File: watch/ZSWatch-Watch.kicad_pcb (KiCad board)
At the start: 4 copper layers, 37.2 x 38 mm, 62 parts, among them IC401 nPM1300-QEXX, IC501 APDS-9306-065, IC502 BMI270, IC503 LIS2MDLTR, IC504 BMP581, IC505 DRV2603RUNT, IC506 PCA9306JK, IC507 RV-8263-C8, IC601 FAN5622SX, IC602 USBLC6-2P6, IC603 MX25U51245GZ4I00, IC604 NTS0104GU12, M601 NORA-B106, X402 Battery, X509 Motor, X603 Device, X608 Display

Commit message: Add speaker
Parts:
- removed R503: 100k, Resistor_SMD:R_0201_0603Metric
- added LS801: Speaker, Same Sky:CMR-12062S-67, F.Cu at (191.8, 143.8)
- C502, MK501: moved to F.Cu
- moved C501 28.8 mm to (220.8, 128.5), turned to 45 degrees
- moved IC501 28.2 mm to (219.7, 127.2), turned to 45 degrees
- moved MK501 25.6 mm to (196.9, 139.6)
- moved C502 23.9 mm to (198.8, 140.8), turned to 90 degrees
- moved C509 20.7 mm to (214.1, 126.4), turned to 0 degrees
- moved C508 19.8 mm to (212.9, 127.2), turned to -90 degrees
- moved IC504 19.8 mm to (214.3, 127.7), turned to 90 degrees
- moved C504 15.9 mm to (210.5, 136.1), turned to -90 degrees
- moved IC502 15.6 mm to (212.2, 135.2), turned to -90 degrees
- moved C503 14.1 mm to (210.5, 134.2), turned to 90 degrees
- moved C506 11.1 mm to (211.1, 132.2), turned to 90 degrees
- moved C505 8.25 mm to (212.6, 130.7), turned to 180 degrees
- moved IC503 8.24 mm to (212.6, 132.2), turned to 180 degrees
- moved IC505 7.66 mm to (199.4, 142.9), turned to 180 degrees
- moved C507 5.86 mm to (214.0, 132.3), turned to -90 degrees
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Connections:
- M601 pad C8: /Project Architecture/MCU/~{RTC-INT} -> /Project Architecture/Extension/PA-BCLK
- M601 pad D3: /Project Architecture/Extension/Status -> /Project Architecture/Extension/~{RESET_{HR}}
- M601 pad E3: /Project Architecture/Extension/~{RESET_{HR}} -> /Project Architecture/Extension/Status
- M601 pad E7: /Project Architecture/Extension/PA-BCLK -> /Project Architecture/MCU/BMI270-INT
- M601 pad F7: unconnected-(M601C-P1.07-PadF7) -> /Project Architecture/MCU/LIS2MDL-INT
- M601 pad F8: /Project Architecture/MCU/MIC-CLK -> unconnected-(M601C-P1.14-PadF8)
- M601 pad F9: /Project Architecture/MCU/MIC-DATA -> /Project Architecture/MCU/~{RTC-INT}
- M601 pad G1: /Project Architecture/MCU/BMI270-INT -> /Project Architecture/MCU/VIB-EN
- M601 pad G2: /Project Architecture/MCU/VIB-EN -> /Project Architecture/MCU/MIC-DATA
- M601 pad G3: unconnected-(M601B-P0.25/AIN4-PadG3) -> /Project Architecture/MCU/MIC-CLK
- M601 pad H7: /Project Architecture/MCU/LIS2MDL-INT -> unconnected-(M601B-P0.29-PadH7)
- M801 pad S11: GND -> Net-(M801-SP_{N})
- M801 pad S112: /Project Architecture/Extension/~{RESET_{HR}} -> /Project Architecture/Extension/Status
- M801 pad S113: (no net) -> GND
- M801 pad S114: /Project Architecture/Extension/Status -> /Project Architecture/Extension/~{RESET_{HR}}
- M801 pad S12: /Project Architecture/Power Management/VSYS -> /Project Architecture/Extension/VHR
- M801 pad S13: (no net) -> Net-(M801-SP_{P})
- M801 pad S14: /Project Architecture/Extension/VHR -> /Project Architecture/Power Management/VSYS
- M801 pad S21: /Project Architecture/Extension/SP_{N} -> (no net)
- M801 pad S23: /Project Architecture/Extension/SP_{P} -> (no net)
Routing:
- net Net-(M801-SP_{P}): track 0.00 -> 19.5 mm, vias 0 -> 1
- net /Project Architecture/MCU/LIS2MDL-INT: track 37.5 -> 20.3 mm, vias 2 -> 3
- net Net-(M801-SP_{N}): track 0.00 -> 14.9 mm, vias 0 -> 1
- net /Project Architecture/Extension/SDA: track 71.2 -> 59.7 mm, vias 5 -> 3
- net /Project Architecture/MCU/BMI270-INT: track 23.4 -> 12.5 mm
- net /Project Architecture/MCU/MIC-CLK: track 13.5 -> 22.7 mm, vias 1 -> 2
- net /Project Architecture/Extension/VHR: track 46.3 -> 38.7 mm
- net /Project Architecture/Extension/SCL: track 70.4 -> 62.8 mm
- net /Project Architecture/MCU/VIB-EN: track 16.5 -> 10.6 mm
- net /Project Architecture/Extension/Status: track 16.8 -> 21.3 mm
- net /Project Architecture/Extension/PA-BCLK: track 14.5 -> 10.4 mm
- net /Project Architecture/Extension/~{RESET_{HR}}: track 21.1 -> 17.2 mm
- net /Project Architecture/MCU/VIB-PWM: track 16.4 -> 13.0 mm
- net /Project Architecture/Power Management/VSYS: track 60.0 -> 56.6 mm
- net USB-D-: track 20.1 -> 18.1 mm
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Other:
- board size 37.2 x 38 mm -> 37.4 x 37.5 mm

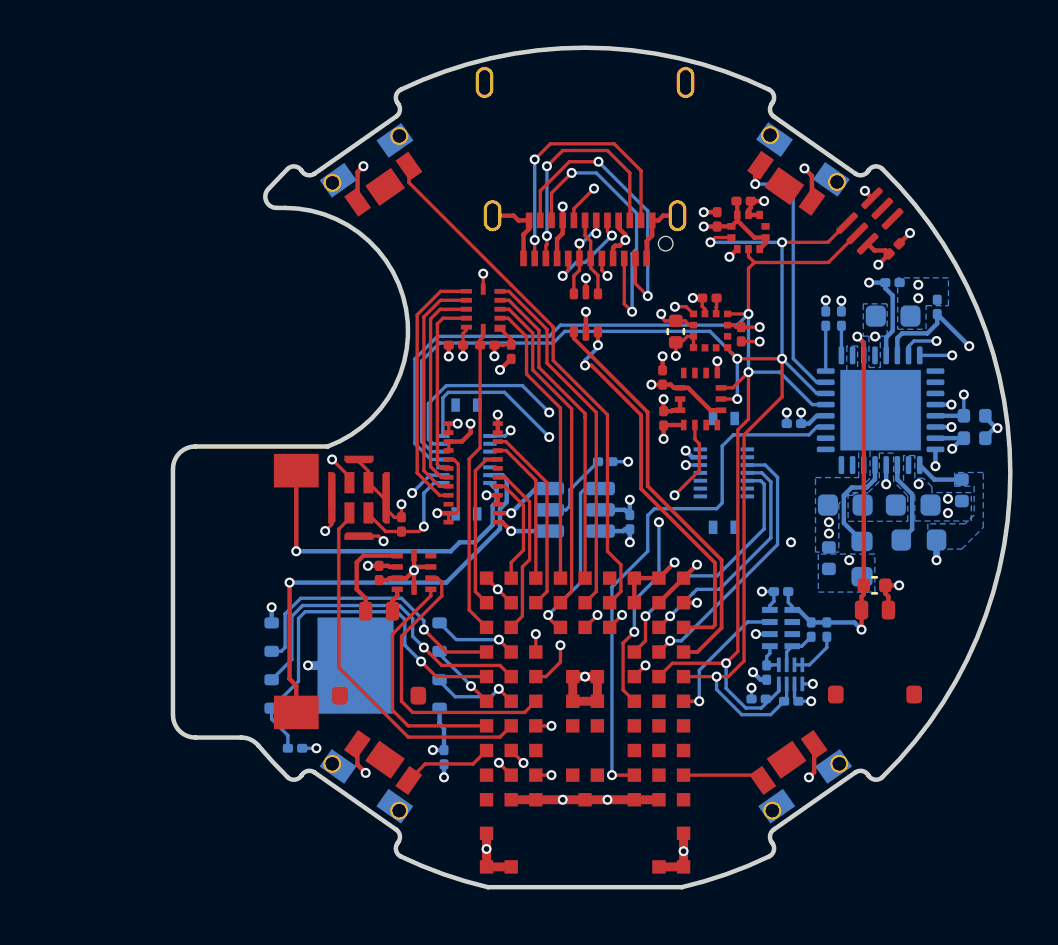
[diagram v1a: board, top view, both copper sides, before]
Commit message: New PCB outline, fix logo copy job for KiBot
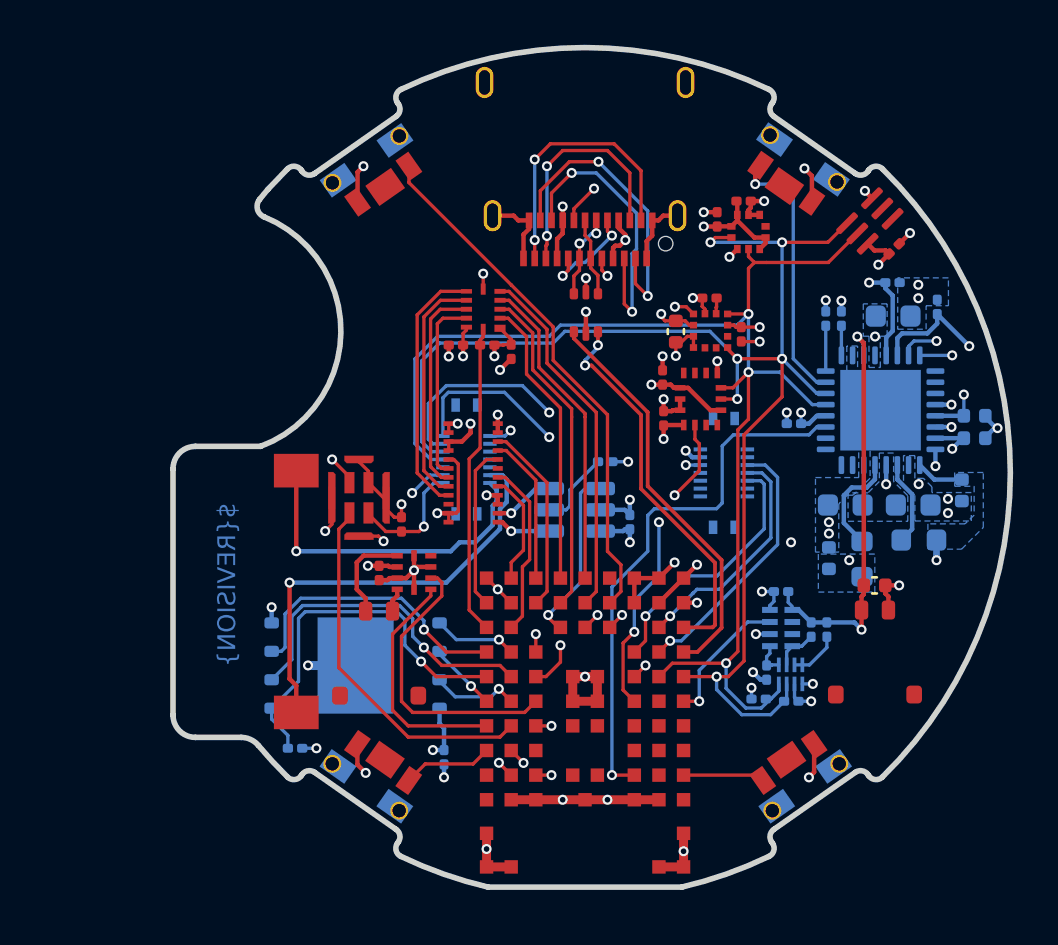
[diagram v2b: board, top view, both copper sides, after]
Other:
- outline, holes or cut-outs redrawn
- board text added: "${REVISION}"

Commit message: Move display connector 3 mm to the outside and optimize routing
Signed-off-by: Daniel Kampert <DanielKampert@kampis-elektroecke.de>
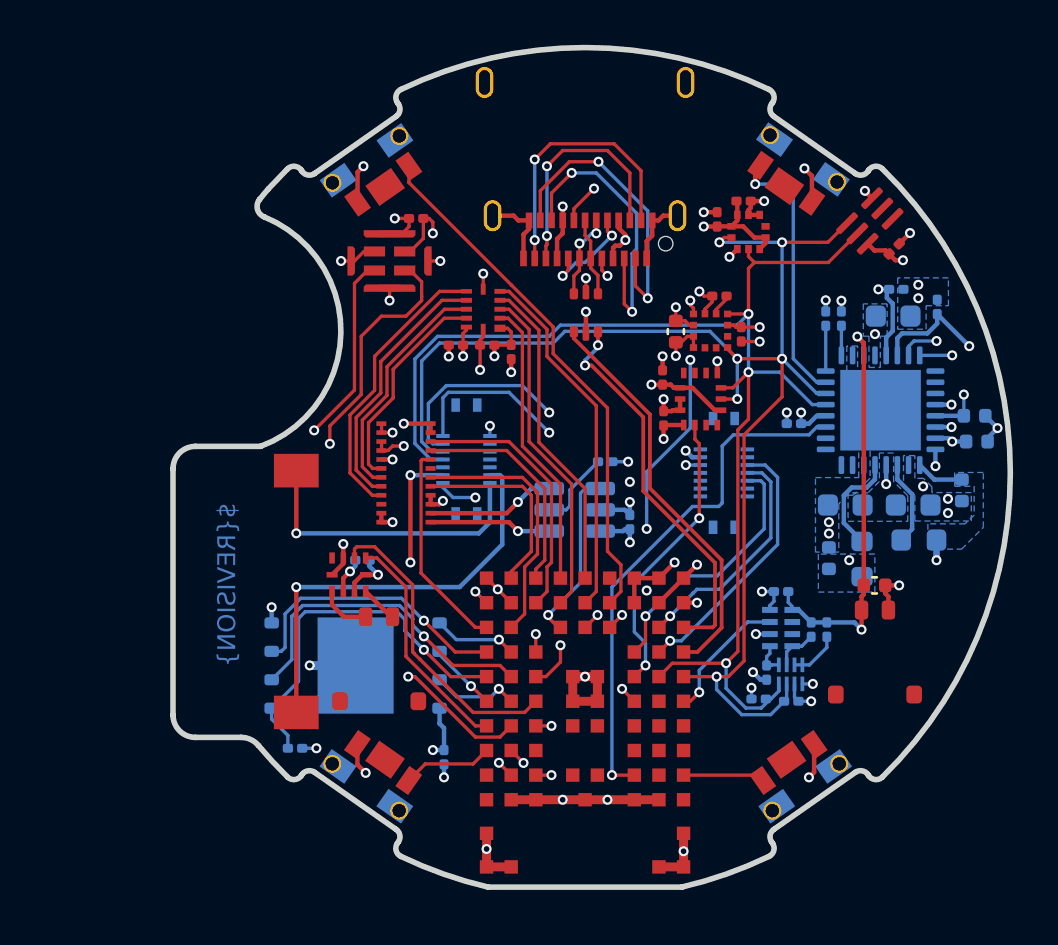
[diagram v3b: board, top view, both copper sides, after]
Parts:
- C510: moved to B.Cu
- moved C502 13.7 mm to (199.5, 127.1), turned to 180 degrees
- moved MK501 10.7 mm to (198.3, 129.0), turned to 90 degrees
- moved X608 3.00 mm to (199.0, 138.5)
- moved IC505 2.91 mm to (196.4, 143.1), turned to -90 degrees
- moved C510 0.94 mm to (197.1, 142.4), turned to 0 degrees
- moved C505 0.45 mm to (213.0, 130.6)
- moved C401 0.34 mm to (220.9, 130.3)
- moved X509 0.25 mm to (197.8, 146.8)
- moved C512 0.18 mm to (224.5, 137.1)
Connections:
- M601 pad B1: DISPLAY-CLK -> DISPLAY-EN
- M601 pad C1: DISPLAY-EN -> DISPLAY-CLK
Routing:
- net /Project Architecture/MCU/MIC-DATA: track 16.3 -> 28.4 mm, vias 0 -> 2
- net /Project Architecture/Extension/VHR: track 38.7 -> 47.7 mm, vias 2 -> 4
- net /Project Architecture/MCU/MIC-CLK: track 22.7 -> 30.7 mm
- net DISPLAY-DC: track 4.98 -> 8.74 mm
- net DISPLAY-DATA: track 7.83 -> 11.6 mm
- net DISPLAY-CS: track 6.62 -> 9.97 mm
- net DISPLAY-RST: track 8.53 -> 11.8 mm
- net GND: track 75.3 -> 72.1 mm, vias 54 -> 56
- net LEDK2: track 2.76 -> 5.76 mm
- net LEDK1: track 2.47 -> 5.47 mm
- net DISPLAY-CLK: track 7.32 -> 9.40 mm
- net Net-(IC505-OUT-): track 4.28 -> 2.32 mm
- net +3V0: track 42.3 -> 44.1 mm
- net Net-(M801-SP_{N}): track 14.9 -> 13.4 mm
- net /Project Architecture/Power Management/VSYS: track 56.6 -> 58.1 mm, vias 6 -> 7
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
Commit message: Fix wrong Extension footprint
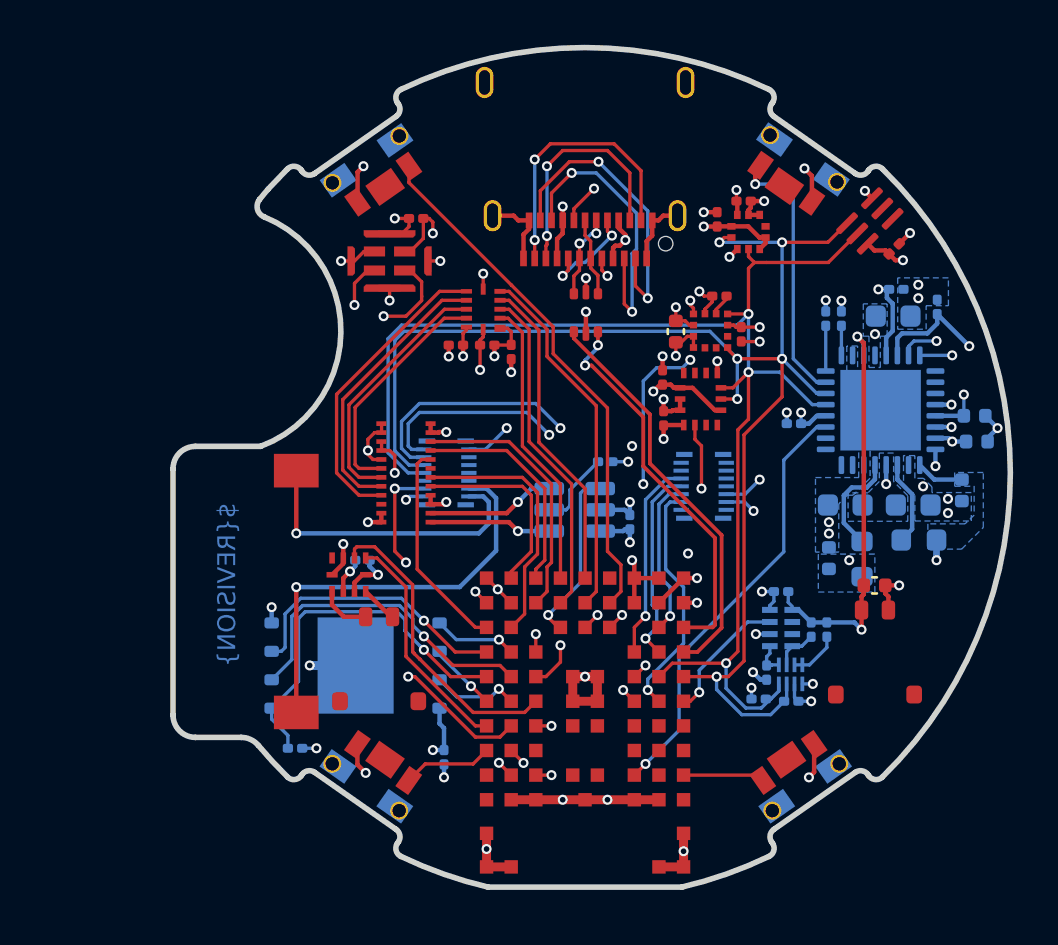
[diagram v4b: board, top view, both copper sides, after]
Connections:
- M601 pad C8: /Project Architecture/Extension/PA-BCLK -> /Project Architecture/Extension/PA-DIN
- M601 pad D8: /Project Architecture/Extension/PA-DIN -> /Project Architecture/Extension/PA-BCLK
- M601 pad F8: unconnected-(M601C-P1.14-PadF8) -> /Project Architecture/Extension/PA-MCLK
- M801 pad S211: (no net) -> /Project Architecture/Extension/PA-MCLK
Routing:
- net /Project Architecture/Extension/PA-MCLK: track 0.00 -> 10.7 mm, vias 0 -> 1
- net /Project Architecture/Extension/PA-DIN: track 11.9 -> 7.09 mm
- net /Project Architecture/MCU/PMIC-INT: track 23.4 -> 19.3 mm
- net /Project Architecture/Extension/SDA: track 59.7 -> 62.2 mm
- net /Project Architecture/Extension/SCL: track 62.0 -> 64.6 mm
- net /Project Architecture/Extension/PA-WCLK: track 11.5 -> 8.99 mm
- net GND: track 72.1 -> 74.6 mm
- net /Project Architecture/Extension/VPA: track 17.0 -> 14.6 mm
- net +3V0: track 44.1 -> 46.3 mm
- net /Project Architecture/Extension/VHR: track 47.7 -> 49.9 mm
- net /Project Architecture/Extension/PA-BCLK: track 10.4 -> 8.82 mm
- net /Project Architecture/Extension/~{RESET_{HR}}: track 17.4 -> 18.6 mm
- net Net-(IC604-B2): track 10.6 -> 11.4 mm
- net Net-(IC604-B1): track 9.56 -> 10.4 mm
- net Net-(IC604-B3): track 11.7 -> 12.5 mm
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
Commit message: New buttons
Signed-off-by: Daniel Kampert <DanielKampert@kampis-elektroecke.de>
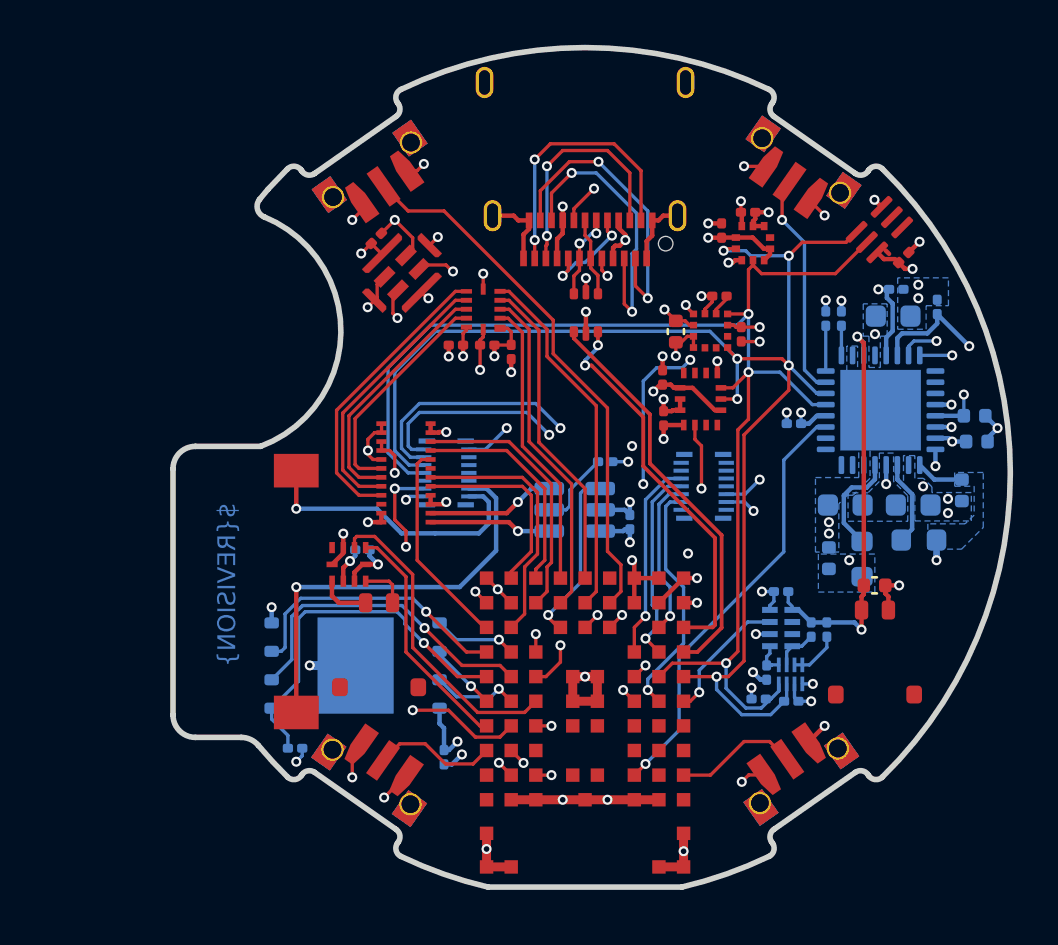
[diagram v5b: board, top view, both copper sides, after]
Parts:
- S501, S502, S503, S504: footprint E-Switch:TL6340AF160Q_Modified -> Wuerth:43633303381_NoMountingPads
- moved C502 1.99 mm to (197.7, 128.0), turned to -135 degrees
- moved MK501 0.77 mm to (198.8, 129.6), turned to 135 degrees
- moved X509 0.62 mm to (197.8, 146.2)
- moved IC501 0.58 mm to (220.1, 127.6)
- moved C501 0.58 mm to (221.2, 128.9)
- moved IC504 0.54 mm to (214.5, 128.2)
- moved C508 0.54 mm to (213.1, 127.7)
- moved C509 0.54 mm to (214.3, 126.9)
- moved C510 0.46 mm to (197.1, 141.9)
- moved IC505 0.46 mm to (196.4, 142.6)
- moved S502 0.46 mm to (216.6, 152.1)
- moved S503 0.40 mm to (197.4, 124.9)
- moved S504 0.39 mm to (197.4, 152.2)
- moved S501 0.20 mm to (216.7, 124.7)
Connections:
- S501 pad 1: /Project Architecture/MCU/SW1 -> GND
- S501 pad 2: GND -> /Project Architecture/MCU/SW1
- S504 pad 1: /Project Architecture/MCU/SW4 -> GND
- S504 pad 2: GND -> /Project Architecture/MCU/SW4
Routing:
- net GND: track 74.6 -> 77.5 mm, vias 56 -> 60
- net /Project Architecture/Extension/VHR: track 49.9 -> 52.0 mm
- net /Project Architecture/MCU/SW2: track 3.64 -> 5.58 mm
- net /Project Architecture/MCU/MIC-DATA: track 28.3 -> 30.2 mm
- net /Project Architecture/MCU/SW1: track 12.0 -> 10.1 mm
- net /Project Architecture/MCU/SW4: track 4.03 -> 5.55 mm
- net /Project Architecture/Extension/SCL: track 64.6 -> 63.7 mm
- net /Project Architecture/Extension/SDA: track 62.2 -> 61.5 mm
- net Net-(M801-SP_{N}): track 13.5 -> 12.9 mm
- net /Project Architecture/MCU/SW3: track 23.6 -> 24.1 mm
